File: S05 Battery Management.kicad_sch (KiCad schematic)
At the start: 17 parts, among them Q10 DMT4011LFG, Q11 DMT4011LFG, Q12 DMP3018SFV, Q13 DMP3018SFV, Q14 DMP3018SFV, Q15 DMP3018SFV, Q8 DMT4011LFG, Q9 DMT4011LFG, U1 LTC1960

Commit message: Use KiCad standard footprints for chip resistors and capacitors
The imported Lattech R/C footprints have poor land patterns (the 0402s
use 0.635 mm circular pads) and cause tombstoning in assembly. Replace
all 139 chip resistors and capacitors with KiCad's standard IPC-7351
nominal footprints:

  Res 0402/0603/1206/2512 -> Resistor_SMD:R_xxxx_xxxxMetric (87)
  Cap 0402/0603/0805/1206/1210 -> Capacitor_SMD:C_xxxx_xxxxMetric (52)

Each part keeps its position, rotation, side, pad nets, schematic link
and reference/value text placement. The pads are on the same axis with
pad 1 on the same side, and every old pad centre lies inside the new
pad, so existing tracks still connect. Zones are refilled.

Schematic Footprint fields and the symbols' footprint filters point at
the new footprints, and the unused imported R/C footprints are removed
from the project library. Electrolytic capacitors are not changed.

DRC: 0 unconnected items, as before. Tracks, vias, zone outlines and
all other footprints are unchanged. 11 courtyard overlaps are new,
because the old footprints had no courtyards.

Co-Authored-By: Claude Opus 5.5 <noreply@anthropic.com>
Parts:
- R22, R24, R25, R26, R27: footprint EVO2513-0_5_0-import-fps:Res 0402 H0-45 R -> Resistor_SMD:R_0402_1005Metric
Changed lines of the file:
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@@
 			)
 		)
-		(property "Footprint" "EVO2513-0_5_0-import-fps:Res 0402 H0-45 R"
+		(property "Footprint" "Resistor_SMD:R_0402_1005Metric"
 			(at 265.43 84.9122 0)
 			(hide yes)
@@
 			)
 		)
-		(property "Footprint" "EVO2513-0_5_0-import-fps:Res 0402 H0-45 R"
+		(property "Footprint" "Resistor_SMD:R_0402_1005Metric"
 			(at 265.43 88.7222 0)
 			(hide yes)
@@
 			)
 		)
-		(property "Footprint" "EVO2513-0_5_0-import-fps:Res 0402 H0-45 R"
+		(property "Footprint" "Resistor_SMD:R_0402_1005Metric"
 			(at 265.43 176.3522 0)
 			(hide yes)
@@
 			)
 		)
-		(property "Footprint" "EVO2513-0_5_0-import-fps:Res 0402 H0-45 R"
+		(property "Footprint" "Resistor_SMD:R_0402_1005Metric"
 			(at 52.07 112.8522 0)
 			(hide yes)
@@
 			)
 		)
-		(property "Footprint" "EVO2513-0_5_0-import-fps:Res 0402 H0-45 R"
+		(property "Footprint" "Resistor_SMD:R_0402_1005Metric"
 			(at 265.43 180.1622 0)
 			(hide yes)

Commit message: Fix schematic ERC issues from the import
ERC across all seven sheets reported 1481 issues from the import:

- Every item sat 43 mil off KiCad's 50 mil connection grid in Y, so new
  wires would not snap to existing pins. Each sheet's contents are
  shifted 7 mil (0.1778 mm) onto the grid; the library symbol
  definitions are untouched and a uniform shift keeps every connection.
  A few wire corners on S06 were off grid on their own (at 6740 mil,
  7620 mil and y 3290 mil); they move to the nearest grid point, which
  removes two 10 mil stubs and moves #PWR065 with its wire.
- Nine wires ran 1.27-2.54 mm past the label sitting on them (ID on S01;
  LDVR1/2 and HDVR1/2 on S06), leaving dangling ends. They are trimmed
  back to the label.
- GND, +12V, +3V3MCU and +5V enter through connector pins, so ERC had
  no power source for them. A PWR_FLAG (#FLG01-#FLG04) sits on each.
- The title-block module name used the Altium formula
  ${COPY(DOCUMENTNAME,5,LENGTH(DOCUMENTNAME)-11)}, which KiCad cannot
  evaluate. Each sheet now carries the title it produced.

ERC: 1481 -> 0. The netlist still matches the PCB's 147 nets.

Update PCB from Schematic was rerun afterwards. It changes metadata only:
footprint filters, unit and pin-function data from the symbols, and the
KiLib_Generator fields dropped from the 139 standard R/C footprints. No
placement or copper changes.

Co-Authored-By: Claude Opus 5.5 <noreply@anthropic.com>
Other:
- note added: "Battery Management"
- note removed: "${COPY(DOCUMENTNAME,5,LENGTH(DOCUMENTNAME)-11)}"

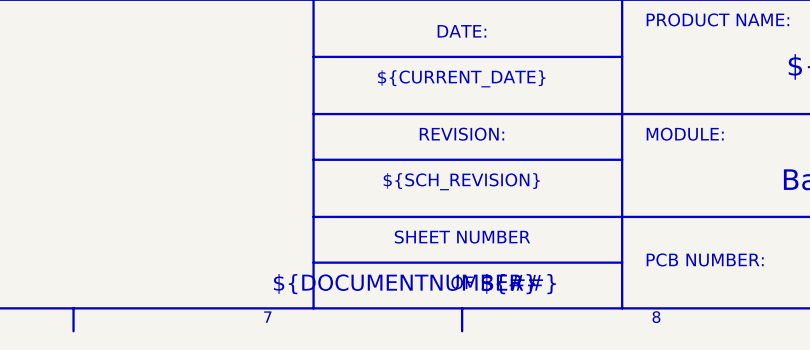
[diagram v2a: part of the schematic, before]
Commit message: Convert the schematic to a hierarchical root sheet
The Altium import produced seven KiCad 10 top-level sheets, with S01's
content in EVO2513-0_5_0.kicad_sch. kicad-cli only loads the first of
those, so command-line ERC, netlist and DRC parity checks saw S01 alone.

- EVO2513-0_5_0.kicad_sch is now a root sheet holding one sheet symbol per
  sheet; S01's content moves to "S01 External Connectors.kicad_sch".
- Each sheet symbol keeps its old top-level sheet UUID, so symbol
  references, net names and connectivity are unchanged: the netlist from
  the new root is identical to the previous whole-design netlist (229
  components, 147 nets). Cross-sheet nets still use global labels.
- The board's 229 footprint paths take the hierarchical form
  /<sheet>/<symbol>, and S01's footprints point at the new sheet file.
  No copper or placement changes.
- Every title block read "sheet 7 of 7" (a single DOCUMENTNUMBER project
  variable). Sheet numbers now use the page number: the root is page 1
  and S01-S07 are pages 2-8.

kicad-cli ERC over the whole design: 0 errors, 0 warnings. DRC with
schematic parity: 0 parity issues, 450 violations as before.

Co-Authored-By: Claude Opus 5.5 <noreply@anthropic.com>
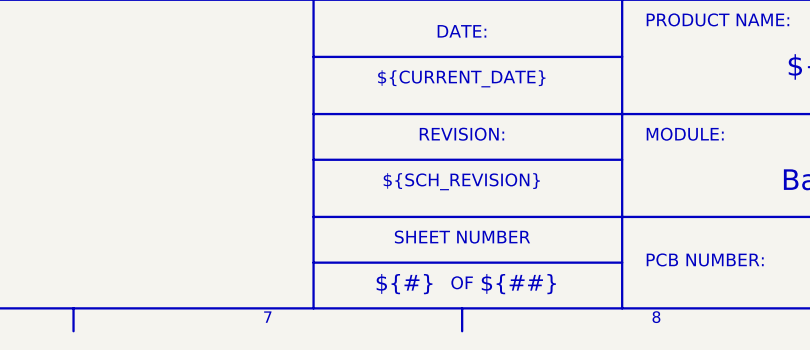
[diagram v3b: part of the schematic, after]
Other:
- note added: "${#}"
- note removed: "${DOCUMENTNUMBER}"
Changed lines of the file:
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@@
 		)
 	)
-	(text "${DOCUMENTNUMBER}"
+	(text "${#}"
 		(exclude_from_sim no)
 		(at 298.45 292.1 0)
@@
 		(instances
 			(project "EVO2513-0_5_0"
-				(path "/bee1e856-8c4d-49a6-b37e-8448f12b694f"
+				(path "/44203427-0a3b-455b-9bb9-c1b577d179b3/bee1e856-8c4d-49a6-b37e-8448f12b694f"
 					(reference "Q13")
 					(unit 1)
@@
 		(instances
 			(project "EVO2513-0_5_0"
-				(path "/bee1e856-8c4d-49a6-b37e-8448f12b694f"
+				(path "/44203427-0a3b-455b-9bb9-c1b577d179b3/bee1e856-8c4d-49a6-b37e-8448f12b694f"
 					(reference "Q10")
 					(unit 1)
@@
 		(instances
 			(project "EVO2513-0_5_0"
-				(path "/bee1e856-8c4d-49a6-b37e-8448f12b694f"
+				(path "/44203427-0a3b-455b-9bb9-c1b577d179b3/bee1e856-8c4d-49a6-b37e-8448f12b694f"
 					(reference "D10")
 					(unit 1)
@@
 		(instances
 			(project "EVO2513-0_5_0"
-				(path "/bee1e856-8c4d-49a6-b37e-8448f12b694f"
+				(path "/44203427-0a3b-455b-9bb9-c1b577d179b3/bee1e856-8c4d-49a6-b37e-8448f12b694f"
 					(reference "R25")
 					(unit 1)
@@
 		(instances
 			(project "EVO2513-0_5_0"
-				(path "/bee1e856-8c4d-49a6-b37e-8448f12b694f"
+				(path "/44203427-0a3b-455b-9bb9-c1b577d179b3/bee1e856-8c4d-49a6-b37e-8448f12b694f"
 					(reference "D9")
 					(unit 1)
@@
 		(instances
 			(project "EVO2513-0_5_0"
-				(path "/bee1e856-8c4d-49a6-b37e-8448f12b694f"
+				(path "/44203427-0a3b-455b-9bb9-c1b577d179b3/bee1e856-8c4d-49a6-b37e-8448f12b694f"
 					(reference "R24")
 					(unit 1)
@@
 		(instances
 			(project "EVO2513-0_5_0"
-				(path "/bee1e856-8c4d-49a6-b37e-8448f12b694f"
+				(path "/44203427-0a3b-455b-9bb9-c1b577d179b3/bee1e856-8c4d-49a6-b37e-8448f12b694f"
 					(reference "#PWR059")
 					(unit 1)
@@
 		(instances
 			(project "EVO2513-0_5_0"
-				(path "/bee1e856-8c4d-49a6-b37e-8448f12b694f"
+				(path "/44203427-0a3b-455b-9bb9-c1b577d179b3/bee1e856-8c4d-49a6-b37e-8448f12b694f"
 					(reference "#PWR056")
 					(unit 1)
@@
 		(instances
 			(project "EVO2513-0_5_0"
-				(path "/bee1e856-8c4d-49a6-b37e-8448f12b694f"
+				(path "/44203427-0a3b-455b-9bb9-c1b577d179b3/bee1e856-8c4d-49a6-b37e-8448f12b694f"
 					(reference "R27")
 					(unit 1)
@@
 		(instances
 			(project "EVO2513-0_5_0"
-				(path "/bee1e856-8c4d-49a6-b37e-8448f12b694f"
+				(path "/44203427-0a3b-455b-9bb9-c1b577d179b3/bee1e856-8c4d-49a6-b37e-8448f12b694f"
 					(reference "#PWR060")
 					(unit 1)
@@
 		(instances
 			(project "EVO2513-0_5_0"
-				(path "/bee1e856-8c4d-49a6-b37e-8448f12b694f"
+				(path "/44203427-0a3b-455b-9bb9-c1b577d179b3/bee1e856-8c4d-49a6-b37e-8448f12b694f"
 					(reference "Q8")
 					(unit 1)
@@
 		(instances
 			(project "EVO2513-0_5_0"
-				(path "/bee1e856-8c4d-49a6-b37e-8448f12b694f"
+				(path "/44203427-0a3b-455b-9bb9-c1b577d179b3/bee1e856-8c4d-49a6-b37e-8448f12b694f"
 					(reference "Q14")
 					(unit 1)
@@
 		(instances
 			(project "EVO2513-0_5_0"
-				(path "/bee1e856-8c4d-49a6-b37e-8448f12b694f"
+				(path "/44203427-0a3b-455b-9bb9-c1b577d179b3/bee1e856-8c4d-49a6-b37e-8448f12b694f"
 					(reference "Q11")
 					(unit 1)
@@
 		(instances
 			(project "EVO2513-0_5_0"
-				(path "/bee1e856-8c4d-49a6-b37e-8448f12b694f"
+				(path "/44203427-0a3b-455b-9bb9-c1b577d179b3/bee1e856-8c4d-49a6-b37e-8448f12b694f"
 					(reference "R22")
 					(unit 1)
@@
 		(instances
 			(project "EVO2513-0_5_0"
-				(path "/bee1e856-8c4d-49a6-b37e-8448f12b694f"
+				(path "/44203427-0a3b-455b-9bb9-c1b577d179b3/bee1e856-8c4d-49a6-b37e-8448f12b694f"
 					(reference "#PWR058")
 					(unit 1)
@@
 		(instances
 			(project "EVO2513-0_5_0"
-				(path "/bee1e856-8c4d-49a6-b37e-8448f12b694f"
+				(path "/44203427-0a3b-455b-9bb9-c1b577d179b3/bee1e856-8c4d-49a6-b37e-8448f12b694f"
 					(reference "U1")
 					(unit 4)
@@
 		(instances
 			(project "EVO2513-0_5_0"
-				(path "/bee1e856-8c4d-49a6-b37e-8448f12b694f"
+				(path "/44203427-0a3b-455b-9bb9-c1b577d179b3/bee1e856-8c4d-49a6-b37e-8448f12b694f"
 					(reference "U1")
 					(unit 5)
@@
 		(instances
 			(project "EVO2513-0_5_0"
-				(path "/bee1e856-8c4d-49a6-b37e-8448f12b694f"
+				(path "/44203427-0a3b-455b-9bb9-c1b577d179b3/bee1e856-8c4d-49a6-b37e-8448f12b694f"
 					(reference "D4")
 					(unit 1)
@@
 		(instances
 			(project "EVO2513-0_5_0"
-				(path "/bee1e856-8c4d-49a6-b37e-8448f12b694f"
+				(path "/44203427-0a3b-455b-9bb9-c1b577d179b3/bee1e856-8c4d-49a6-b37e-8448f12b694f"
 					(reference "Q9")
 					(unit 1)
@@
 		(instances
 			(project "EVO2513-0_5_0"
-				(path "/bee1e856-8c4d-49a6-b37e-8448f12b694f"
+				(path "/44203427-0a3b-455b-9bb9-c1b577d179b3/bee1e856-8c4d-49a6-b37e-8448f12b694f"
 					(reference "Q12")
 					(unit 1)
@@
 		(instances
 			(project "EVO2513-0_5_0"
-				(path "/bee1e856-8c4d-49a6-b37e-8448f12b694f"
+				(path "/44203427-0a3b-455b-9bb9-c1b577d179b3/bee1e856-8c4d-49a6-b37e-8448f12b694f"
 					(reference "#PWR057")
 					(unit 1)
@@
 		(instances
 			(project "EVO2513-0_5_0"
-				(path "/bee1e856-8c4d-49a6-b37e-8448f12b694f"
+				(path "/44203427-0a3b-455b-9bb9-c1b577d179b3/bee1e856-8c4d-49a6-b37e-8448f12b694f"
 					(reference "Q15")
 					(unit 1)
@@
 		(instances
 			(project "EVO2513-0_5_0"
-				(path "/bee1e856-8c4d-49a6-b37e-8448f12b694f"
+				(path "/44203427-0a3b-455b-9bb9-c1b577d179b3/bee1e856-8c4d-49a6-b37e-8448f12b694f"
 					(reference "R26")
 					(unit 1)
@@
 		)
 	)
-	(sheet_instances
-		(path "/"
-			(page "5")
-		)
-	)

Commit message: Link the sheets through hierarchical labels and sheet pins
The 78 cross-sheet global labels on S01-S07 become hierarchical labels,
and each sheet symbol on the root gets a pin per label name (71 pins).
On the root, each pin connects through a short wire to a global label
with the net name. Global labels there, rather than local ones, keep the
35 net names free of a "/" sheet-path prefix, so the net classes and the
board's nets are unchanged.

Layout: S01 External Connectors on the left with its pins on the right
edge; S02-S04 and S05-S07 in two columns with their pins on the left.

The netlist is identical to before (229 components, 147 nets, same names
and pins). kicad-cli ERC: 0 errors, 0 warnings. DRC with schematic
parity: 0 parity issues, 450 violations as before.

Co-Authored-By: Claude Opus 5.5 <noreply@anthropic.com>
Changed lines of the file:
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@@
 		)
 	)
-	(global_label "DCPATH"
+	(hierarchical_label "DCPATH"
 		(shape passive)
 		(at 245.11 151.13 0)
-		(fields_autoplaced yes)
 		(effects
 			(font
@@
 			(justify left)
 		)
-		(property "Intersheetrefs" "${INTERSHEET_REFS}"
-			(at 245.11 151.13 0)
-			(effects
-				(font
-					(size 1.27 1.27)
-				)
-				(justify left)
-				(hide yes)
-			)
-		)
 	)
-	(global_label "CLOCK2"
+	(hierarchical_label "CLOCK2"
 		(shape passive)
 		(at 232.41 180.34 180)
-		(fields_autoplaced yes)
 		(effects
 			(font
@@
 			(justify right)
 		)
-		(property "Intersheetrefs" "${INTERSHEET_REFS}"
-			(at 232.41 180.34 0)
-			(effects
-				(font
-					(size 1.27 1.27)
-				)
-				(justify right)
-				(hide yes)
-			)
-		)
 	)
-	(global_label "SCL2"
+	(hierarchical_label "SCL2"
 		(shape passive)
 		(at 361.95 157.48 0)
-		(fields_autoplaced yes)
 		(effects
 			(font
@@
 			(justify left)
 		)
-		(property "Intersheetrefs" "${INTERSHEET_REFS}"
-			(at 361.95 157.48 0)
-			(effects
-				(font
-					(size 1.27 1.27)
-				)
-				(justify left)
-				(hide yes)
-			)
-		)
 	)
-	(global_label "DSDA1"
+	(hierarchical_label "DSDA1"
 		(shape passive)
 		(at 361.95 71.12 0)
-		(fields_autoplaced yes)
 		(effects
 			(font
@@
 			(justify left)
 		)
-		(property "Intersheetrefs" "${INTERSHEET_REFS}"
-			(at 361.95 71.12 0)
-			(effects
-				(font
-					(size 1.27 1.27)
-				)
-				(justify left)
-				(hide yes)
-			)
-		)
 	)
-	(global_label "SAFE2"
+	(hierarchical_label "SAFE2"
 		(shape passive)
 		(at 359.41 204.47 0)
-		(fields_autoplaced yes)
 		(effects
 			(font
@@
 			(justify left)
 		)
-		(property "Intersheetrefs" "${INTERSHEET_REFS}"
-			(at 359.41 204.47 0)
-			(effects
-				(font
-					(size 1.27 1.27)
-				)
-				(justify left)
-				(hide yes)
-			)
-		)
 	)
-	(global_label "POS1"
+	(hierarchical_label "POS1"
 		(shape passive)
 		(at 26.67 95.25 180)
-		(fields_autoplaced yes)
 		(effects
 			(font
@@
 			(justify right)
 		)
-		(property "Intersheetrefs" "${INTERSHEET_REFS}"
-			(at 26.67 95.25 0)
-			(effects
-				(font
-					(size 1.27 1.27)
-				)
-				(justify right)
-				(hide yes)
-			)
-		)
 	)
-	(global_label "DCPATH"
+	(hierarchical_label "DCPATH"
 		(shape passive)
 		(at 246.38 59.69 0)
-		(fields_autoplaced yes)
 		(effects
 			(font
@@
 			(justify left)
 		)
-		(property "Intersheetrefs" "${INTERSHEET_REFS}"
-			(at 246.38 59.69 0)
-			(effects
-				(font
-					(size 1.27 1.27)
-				)
-				(justify left)
-				(hide yes)
-			)
-		)
 	)
-	(global_label "DCCHARGER"
+	(hierarchical_label "DCCHARGER"
 		(shape passive)
 		(at 27.94 59.69 180)
-		(fields_autoplaced yes)
 		(effects
 			(font
@@
 			(justify right)
 		)
-		(property "Intersheetrefs" "${INTERSHEET_REFS}"
-			(at 27.94 59.69 0)
-			(effects
-				(font
-					(size 1.27 1.27)
-				)
-				(justify right)
-				(hide yes)
-			)
-		)
 	)
-	(global_label "SAFE1"
+	(hierarchical_label "SAFE1"
 		(shape passive)
 		(at 232.41 92.71 180)
-		(fields_autoplaced yes)
 		(effects
 			(font
@@
 			(justify right)
 		)
-		(property "Intersheetrefs" "${INTERSHEET_REFS}"
-			(at 232.41 92.71 0)
-			(effects
-				(font
-					(size 1.27 1.27)
-				)
-				(justify right)
-				(hide yes)
-			)
-		)
 	)
-	(global_label "SAFE1"
+	(hierarchical_label "SAFE1"
 		(shape passive)
 		(at 359.41 113.03 0)
-		(fields_autoplaced yes)
 		(effects
 			(font
@@
 			(justify left)
 		)
-		(property "Intersheetrefs" "${INTERSHEET_REFS}"
-			(at 359.41 113.03 0)
-			(effects
-				(font
-					(size 1.27 1.27)
-				)
-				(justify left)
-				(hide yes)
-			)
-		)
 	)
-	(global_label "DCCHARGER"
+	(hierarchical_label "DCCHARGER"
 		(shape passive)
 		(at 26.67 151.13 180)
-		(fields_autoplaced yes)
 		(effects
 			(font
@@
 			(justify right)
 		)
-		(property "Intersheetrefs" "${INTERSHEET_REFS}"
-			(at 26.67 151.13 0)
-			(effects
-				(font
-					(size 1.27 1.27)
-				)
-				(justify right)
-				(hide yes)
-			)
-		)
 	)
-	(global_label "SAFE2"
+	(hierarchical_label "SAFE2"
 		(shape passive)
 		(at 232.41 184.15 180)
-		(fields_autoplaced yes)
 		(effects
 			(font
@@
 			(justify right)
 		)
-		(property "Intersheetrefs" "${INTERSHEET_REFS}"
-			(at 232.41 184.15 0)
-			(effects
-				(font
-					(size 1.27 1.27)
-				)
-				(justify right)
-				(hide yes)
-			)
-		)
 	)
-	(global_label "SCL1"
+	(hierarchical_label "SCL1"
 		(shape passive)
 		(at 361.95 66.04 0)
-		(fields_autoplaced yes)
 		(effects
 			(font
@@
 			(justify left)
 		)
-		(property "Intersheetrefs" "${INTERSHEET_REFS}"
-			(at 361.95 66.04 0)
-			(effects
-				(font
-					(size 1.27 1.27)
-				)
-				(justify left)
-				(hide yes)
-			)
-		)
 	)
-	(global_label "POS2"
+	(hierarchical_label "POS2"
 		(shape passive)
 		(at 26.67 186.69 180)
-		(fields_autoplaced yes)
 		(effects
 			(font
@@
 			(justify right)
 		)
-		(property "Intersheetrefs" "${INTERSHEET_REFS}"
-			(at 26.67 186.69 0)
-			(effects
-				(font
-					(size 1.27 1.27)
-				)
-				(justify right)
-				(hide yes)
-			)
-		)
 	)
-	(global_label "DSDA2"
+	(hierarchical_label "DSDA2"
 		(shape passive)
 		(at 361.95 162.56 0)
-		(fields_autoplaced yes)
 		(effects
 			(font
@@
 			(justify left)
 		)
-		(property "Intersheetrefs" "${INTERSHEET_REFS}"
-			(at 361.95 162.56 0)
-			(effects
-				(font
-					(size 1.27 1.27)
-				)
-				(justify left)
-				(hide yes)
-			)
-		)
 	)
-	(global_label "CLOCK1"
+	(hierarchical_label "CLOCK1"
 		(shape passive)
 		(at 232.41 88.9 180)
-		(fields_autoplaced yes)
 		(effects
 			(font
@@
 			(justify right)
 		)
-		(property "Intersheetrefs" "${INTERSHEET_REFS}"
-			(at 232.41 88.9 0)
-			(effects
-				(font
-					(size 1.27 1.27)
-				)
-				(justify right)
-				(hide yes)
-			)
-		)
 	)
-	(global_label "DATA2"
+	(hierarchical_label "DATA2"
 		(shape passive)
 		(at 232.41 176.53 180)
-		(fields_autoplaced yes)
 		(effects
 			(font
@@
 			(justify right)
 		)
-		(property "Intersheetrefs" "${INTERSHEET_REFS}"
-			(at 232.41 176.53 0)
-			(effects
-				(font
-					(size 1.27 1.27)
-				)
-				(justify right)
-				(hide yes)
-			)
-		)
 	)
-	(global_label "DATA1"
+	(hierarchical_label "DATA1"
 		(shape passive)
 		(at 232.41 85.09 180)
-		(fields_autoplaced yes)
 		(effects
 			(font
@@
 			(justify right)
 		)
-		(property "Intersheetrefs" "${INTERSHEET_REFS}"
-			(at 232.41 85.09 0)
-			(effects
-				(font
-					(size 1.27 1.27)
-				)
-				(justify right)
-				(hide yes)
-			)
-		)
 	)
